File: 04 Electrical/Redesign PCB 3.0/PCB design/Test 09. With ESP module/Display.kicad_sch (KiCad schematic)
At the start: 1 part, among them U5 ILI9341_no_touch

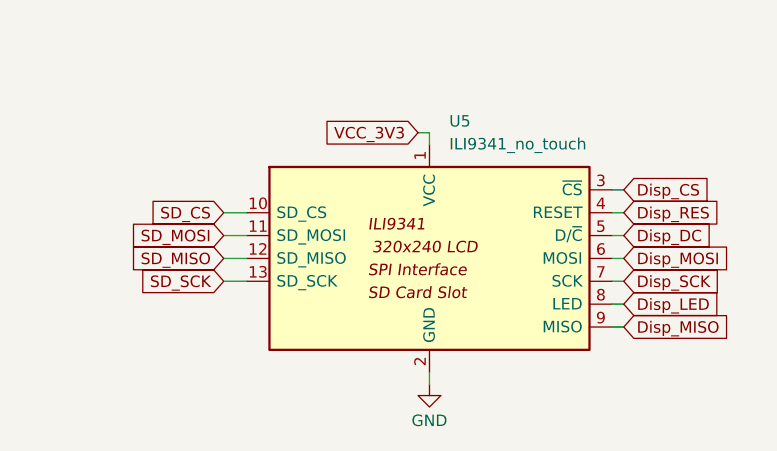
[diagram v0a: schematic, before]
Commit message: Logo added to PCB
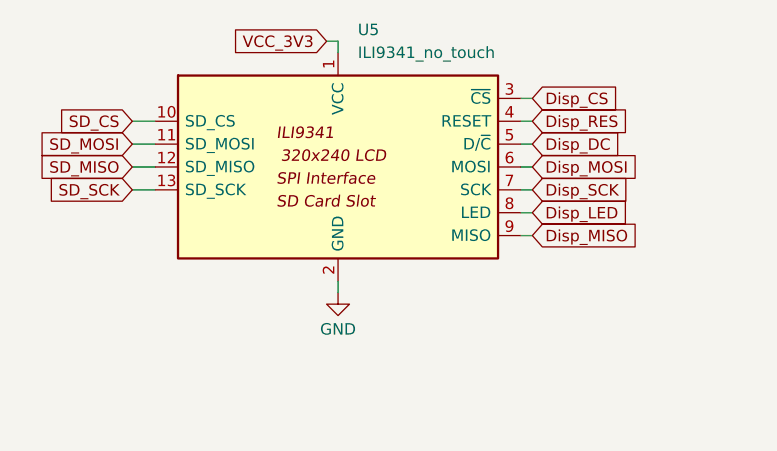
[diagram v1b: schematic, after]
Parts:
- U5: footprint Project:ILI9341_no_touch -> Project:ILI9341_no_touch_no_mount
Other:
- moved on the sheet: U5

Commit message: As ordered at JLCPCB
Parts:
- U5: now not fitted
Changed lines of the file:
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@@
 		(on_board yes)
 		(dnp no)
-		(property "Reference" "#PWR029"
+		(property "Reference" "#PWR027"
 			(at 147.32 107.95 0)
 			(effects
@@
 			(project "Test 09. With ESP module"
 				(path "/dee7d3c3-6abb-4cb3-8df4-3e3e37989a04/4ee7237d-7490-448a-a94f-f4ace25b8494"
-					(reference "#PWR029")
+					(reference "#PWR027")
 					(unit 1)
 				)
@@
 		(in_bom yes)
 		(on_board yes)
-		(dnp no)
+		(dnp yes)
 		(fields_autoplaced yes)
 		(property "Reference" "U5"
@@
 			(at 147.32 93.98 0)
 			(effects
+				(font
+					(size 1.27 1.27)
+				)
+				(hide yes)
+			)
+		)
+		(property "Comment" ""
+			(at 147.32 93.98 0)
+			(effects
